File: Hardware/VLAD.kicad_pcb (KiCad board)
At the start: 2 copper layers, 90 x 90 mm, 99 parts, among them J1 BMP388, J2 BNO055, J3 Micro_SD_Card, J4 Conn_01x02_Male, J5 Conn_01x03_Male, P1 USB_C_Plug_USB2.0, Q1 S8050, Q2 S8050, Q3 S8550, Q4 S8550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

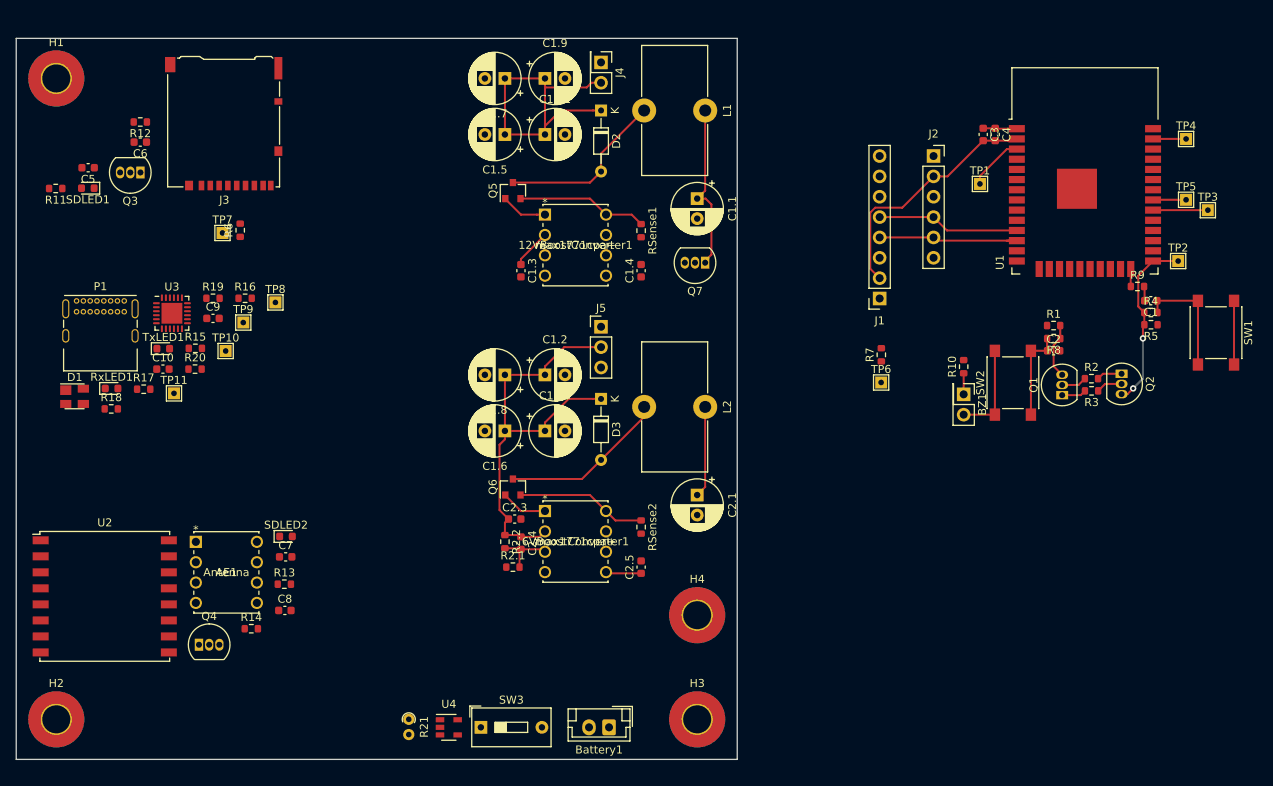
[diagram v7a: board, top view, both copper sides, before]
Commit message: Put EVERYTHING in the 90x90 space
Ofc need to sort out the rats nest better. Nearly there
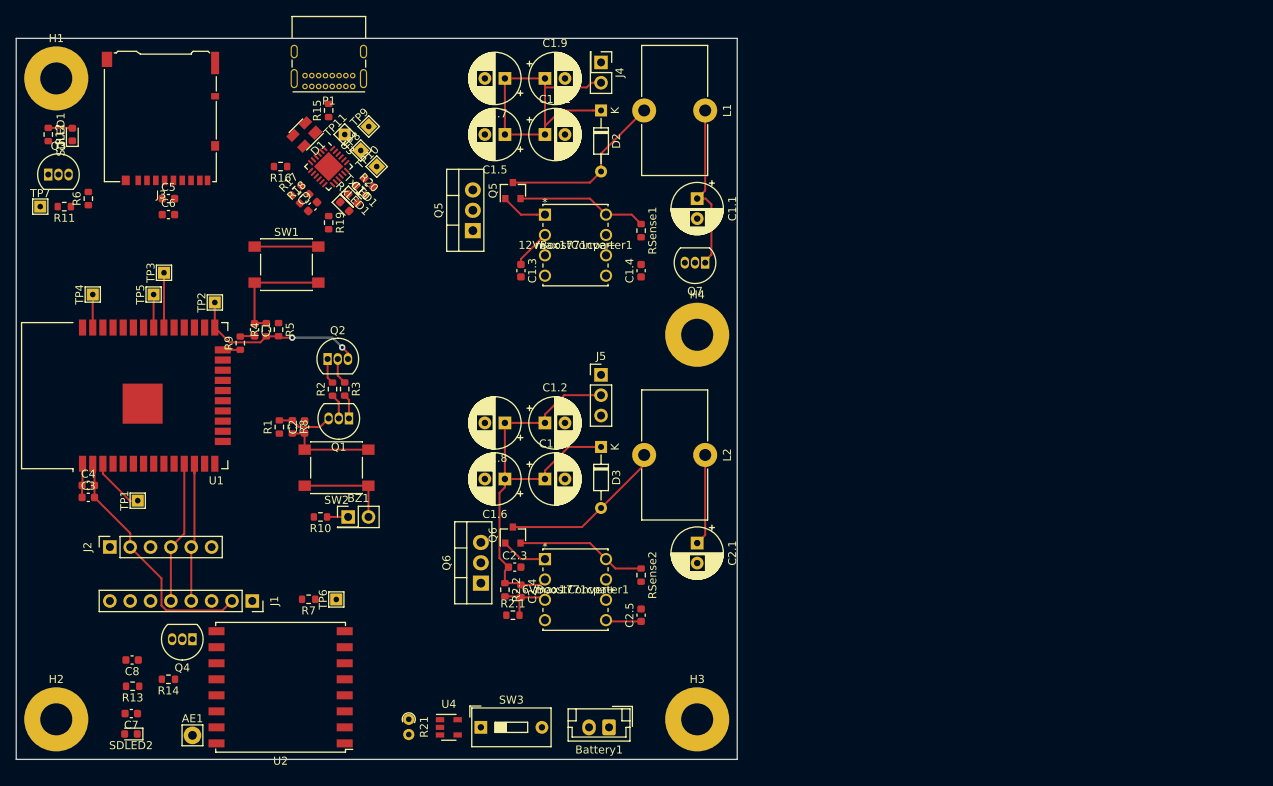
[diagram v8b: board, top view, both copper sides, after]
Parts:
- added Q5: MTP3055VL, Package_TO_SOT_THT:TO-220-3_Vertical, F.Cu at (77.0, 44.0)
- added Q6: MTP3055VL, Package_TO_SOT_THT:TO-220-3_Vertical, F.Cu at (78.0, 88.0)
- AE1: footprint footprints:max1771cpa&plus_ -> Connector_Pin:Pin_D1.1mm_L8.5mm_W2.5mm_FlatFork
- H1, H2, H3, H4: footprint MountingHole:MountingHole_3.5mm_Pad_TopBottom -> MountingHole:MountingHole_4mm_Pad
- moved TP4 137.8 mm to (29.6, 52.0), turned to 90 degrees
- moved TP3 130.5 mm to (38.4, 49.3), turned to 90 degrees
- moved TP5 129.4 mm to (37.1, 52.0), turned to 90 degrees
- moved C4 121.4 mm to (29.0, 75.8), turned to 0 degrees
- moved C3 120.5 mm to (29.0, 77.3), turned to 0 degrees
- moved TP2 120.4 mm to (44.8, 53.0), turned to 90 degrees
- moved U1 119.5 mm to (36.5, 64.6), turned to 90 degrees
- moved SW1 116.3 mm to (53.7, 48.2), turned to 0 degrees
- moved J2 113.8 mm to (31.7, 83.5), turned to 90 degrees
- moved TP1 112.3 mm to (35.2, 77.7), turned to 90 degrees
- moved R9 112.2 mm to (48.0, 58.0), turned to 90 degrees
- moved C1 111.9 mm to (49.7, 56.4), turned to 270 degrees
- moved R4 110.4 mm to (51.2, 56.4), turned to 90 degrees
- moved R5 108.9 mm to (52.7, 56.4), turned to 270 degrees
- moved Q2 99.1 mm to (58.9, 60.0), turned to 0 degrees
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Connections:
- 12VBoostConverter1 pad 1: Net-(12VBoostConverter1-Pad1) -> /Power/Gate1
- 12VBoostConverter1 pad 8: Net-(12VBoostConverter1-Pad8) -> /Power/Source1
- 6VBoostConverter1 pad 1: Net-(6VBoostConverter1-Pad1) -> /Power/Gate2
- 6VBoostConverter1 pad 8: Net-(6VBoostConverter1-Pad8) -> /Power/Source2
- D2 pad 2: Net-(D2-Pad2) -> /Power/Drain1
- D3 pad 2: Net-(D3-Pad2) -> /Power/Drain2
- J5 pad 1: Net-(J5-Pad1) -> /ServoPin
- L1 pad 2: Net-(D2-Pad2) -> /Power/Drain1
- L2 pad 2: Net-(D3-Pad2) -> /Power/Drain2
- RSense1 pad 1: Net-(12VBoostConverter1-Pad8) -> /Power/Source1
- RSense2 pad 1: Net-(6VBoostConverter1-Pad8) -> /Power/Source2
- U1 pad 33: Net-(U1-Pad33) -> /ServoPin
- U1 pad 9: Net-(U1-Pad9) -> 12VBusSwitch
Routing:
- net Net-(R12-Pad1): track 0.00 -> 3.02 mm
